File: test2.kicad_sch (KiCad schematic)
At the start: 24 parts, among them IC1 2EDN8534FXTMA1, J10 Master, J6 XT 60, J8 XT 60, J9 FCCU, Q1 IRFP4468PBF, Q2 IRLIZ44N, Q3 IRLIZ44N, Q4 IRFP4468PBF, U1 HO 25-P

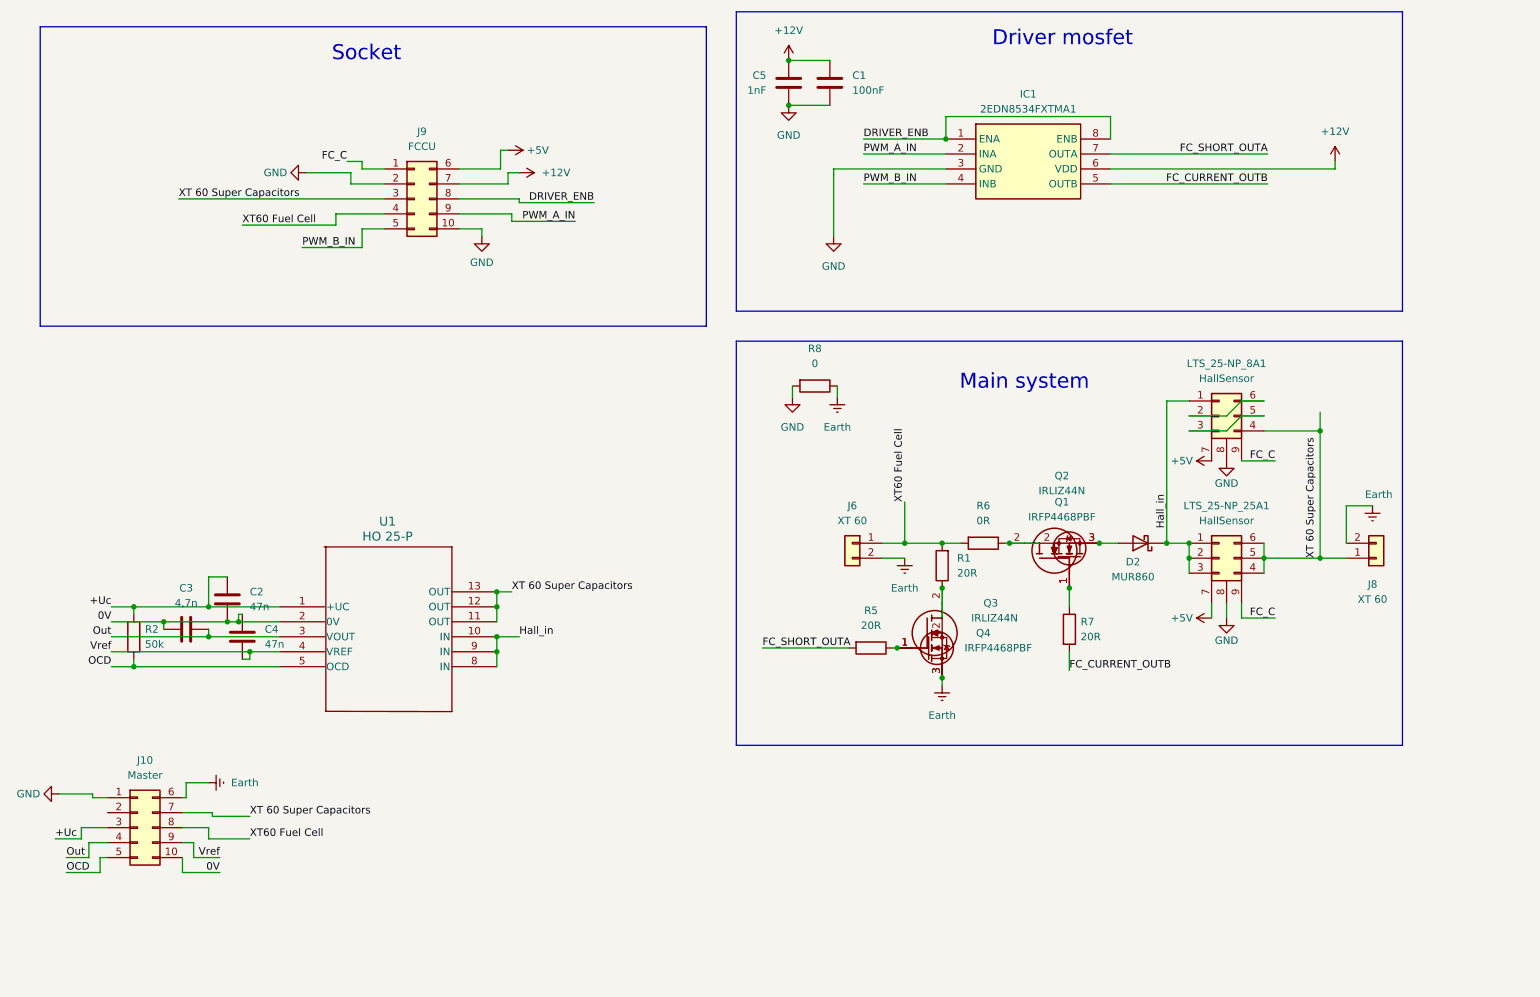
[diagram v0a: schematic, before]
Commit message: Add 3d models
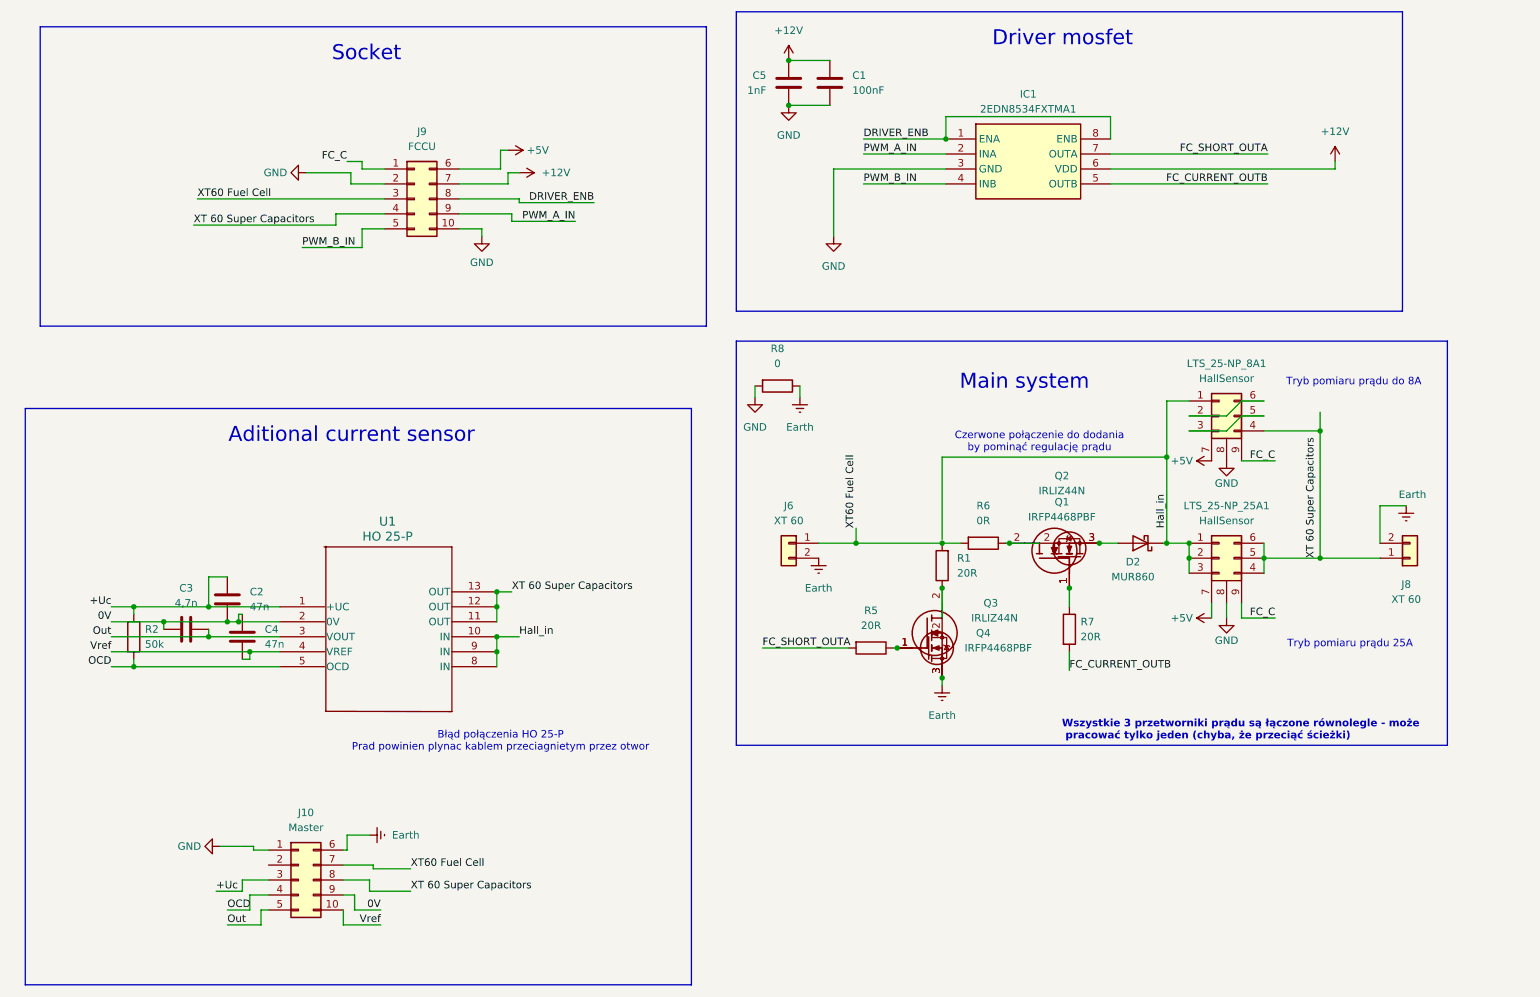
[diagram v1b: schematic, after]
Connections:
- net 0V: now also J10.9 (Pin_9); no longer J10.10 (Pin_10)
- net OCD: now also J10.4 (Pin_4); no longer J10.5 (Pin_5)
- net Out: now also J10.5 (Pin_5); no longer J10.4 (Pin_4)
- net Vref: now also J10.10 (Pin_10); no longer J10.9 (Pin_9)
- net XT 60 Super Capacitors: now also J10.8 (Pin_8), J9.4 (Pin_4); no longer J10.7 (Pin_7), J9.3 (Pin_3)
- net XT60 Fuel Cell: now also J10.7 (Pin_7), J9.3 (Pin_3); no longer J10.8 (Pin_8), J9.4 (Pin_4)
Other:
- note added: "Aditional current sensor"
- note added: "Błąd połączenia HO 25-P Prad powinien plynac kablem przeciagnietym przez otwor"
- note added: "Czerwone połączenie do dodania by pominąć regulację prądu"
- note added: "Tryb pomiaru prądu 25A"
- note added: "Tryb pomiaru prądu do 8A"
- note added: "Wszystkie 3 przetworniki prądu są łączone równolegle - może pracować tylko jeden (chyba, że przeciąć ścieżki)"
- moved on the sheet: J10, J6, J8, R8
